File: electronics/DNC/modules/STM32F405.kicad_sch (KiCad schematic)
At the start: 10 parts

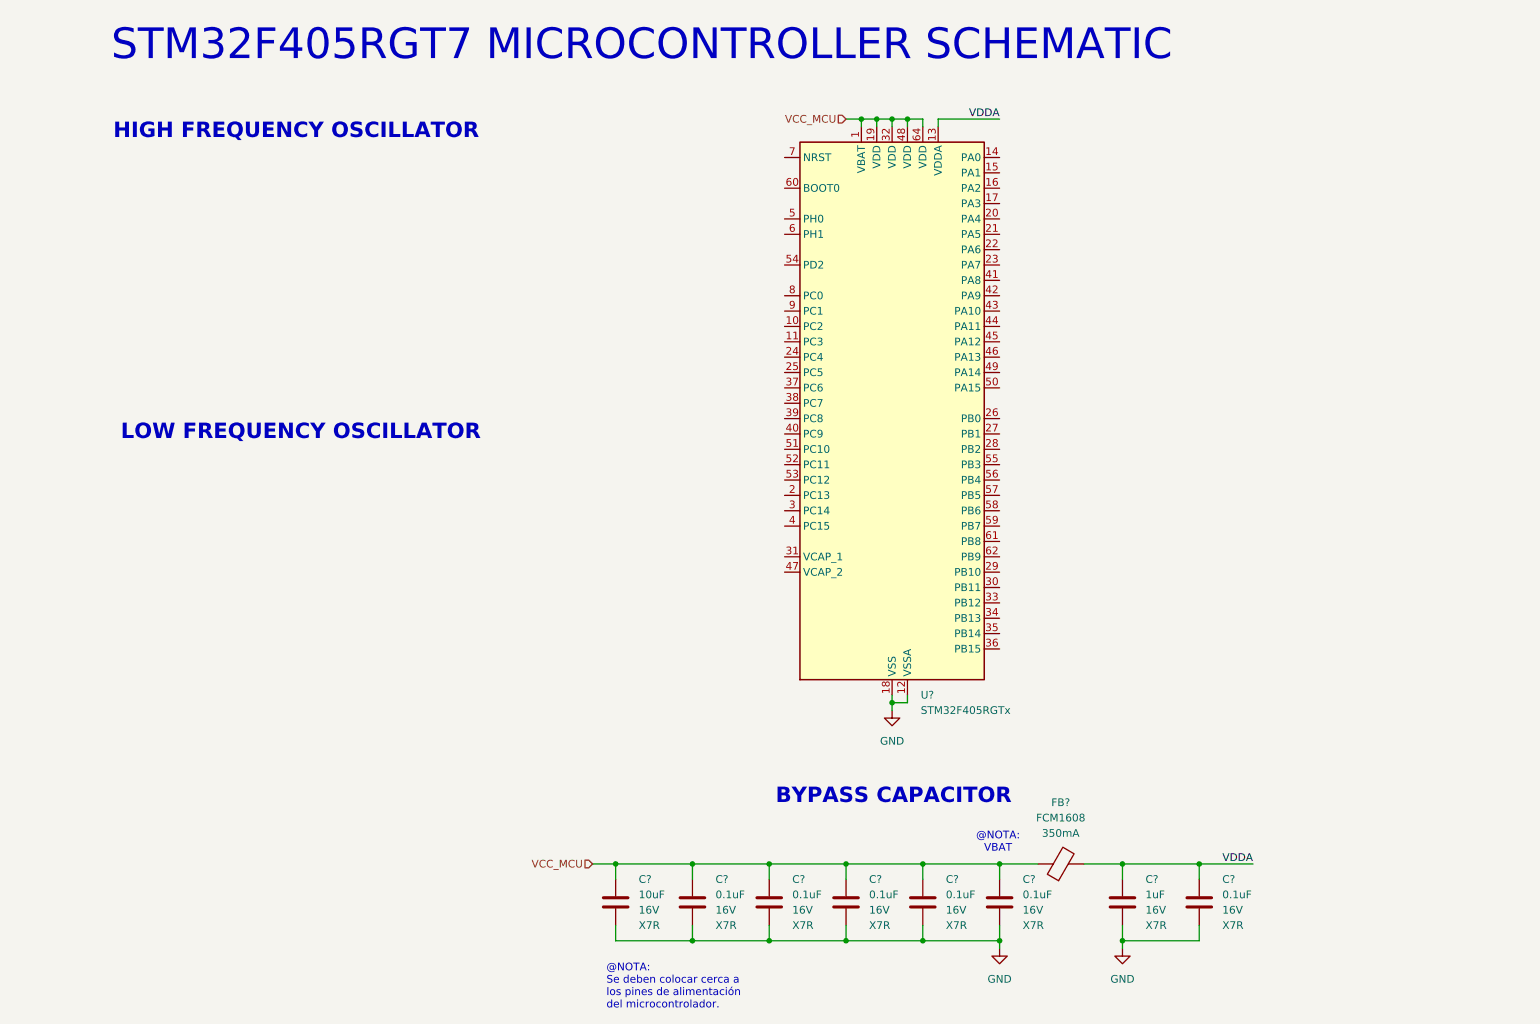
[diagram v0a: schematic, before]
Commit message: Se avanzó con el diseño del DNC y se agregó el modelo 3D del brazo del dron para imprimir
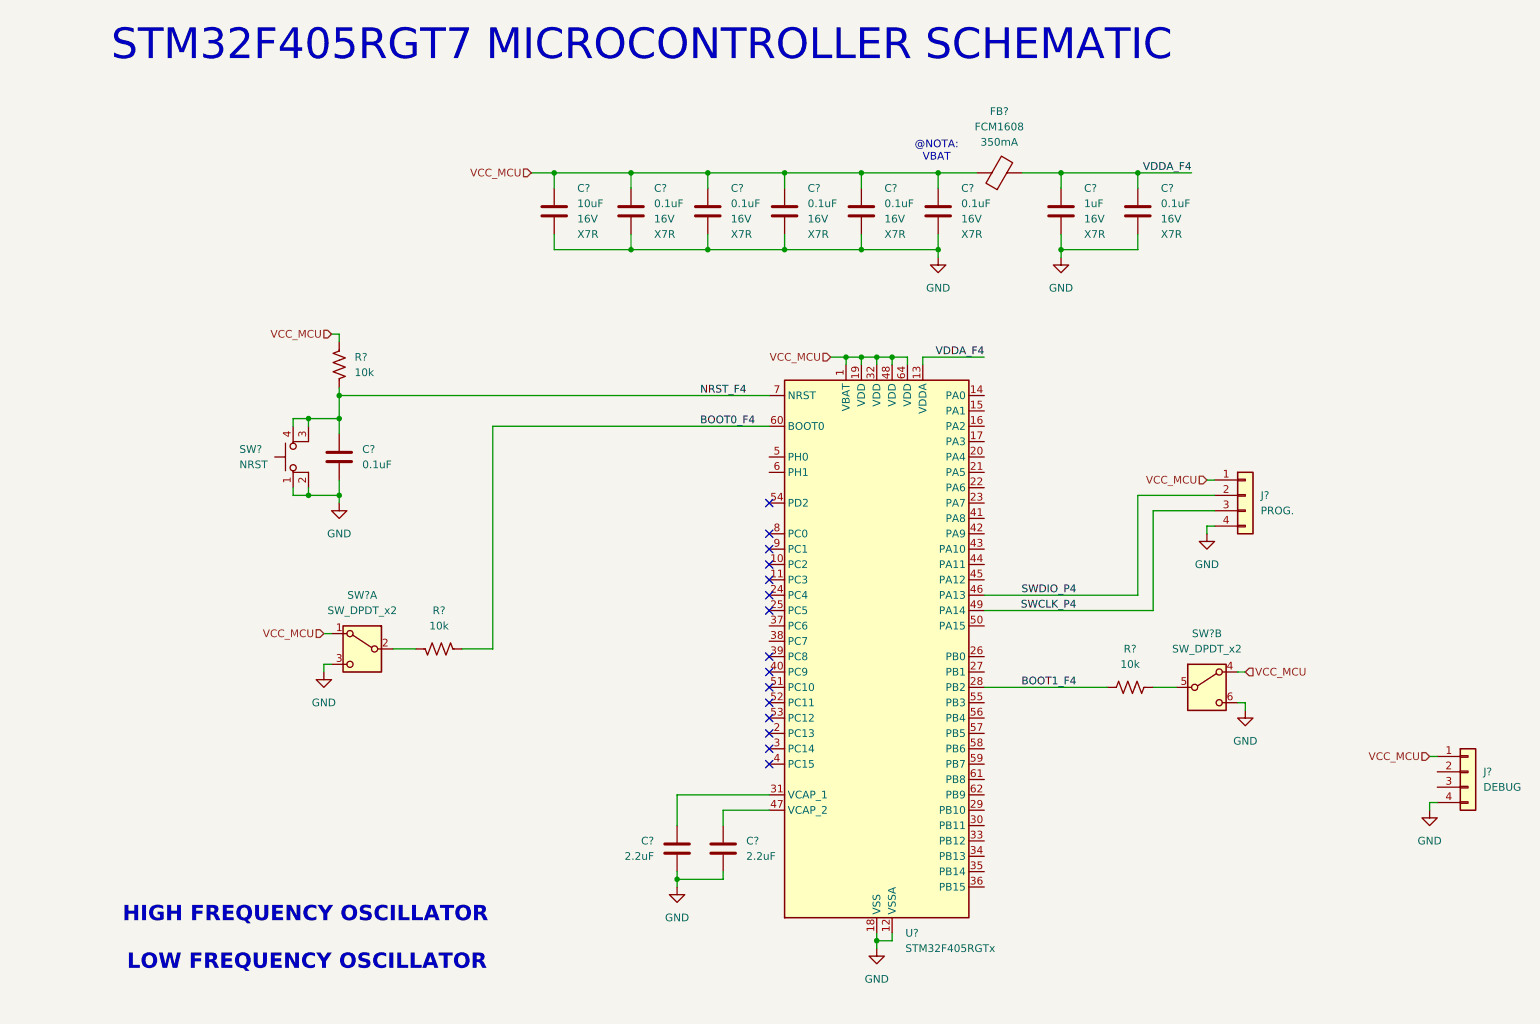
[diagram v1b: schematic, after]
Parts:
- added C? (x2): 2.2uF, symbol Device:C
- added C?: 0.1uF, symbol Device:C
- added J?: PROG., symbol Connector_Generic:Conn_01x04
- added J?: DEBUG, symbol Connector_Generic:Conn_01x04
- added R? (x3): 10k, symbol Device:R_US
- added SW?: NRST, symbol Switch:SW_MEC_5E
- added SW? (x2): SW_DPDT_x2, symbol Switch:SW_DPDT_x2
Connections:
- net GND: now also C?.2, C?.2, C?.2, J?.4 (Pin_4), J?.4 (Pin_4), SW?.1, SW?.2, SW?.3 (C), SW?.6 (C)
- net VCC_MCU: now also J?.1 (Pin_1), J?.1 (Pin_1), R?.1, SW?.1 (A), SW?.4 (A)
- net BOOT1_F4: now reaches U?.28 (PB2)
- net BOOT1_F4: now also R?.1
- net at U?.31 (VCAP_1): now also C?.1
- net SWDIO_P4: now reaches U?.46 (PA13)
- net SWDIO_P4: now also J?.2 (Pin_2)
- net at U?.47 (VCAP_2): now also C?.1
- net SWCLK_P4: now reaches U?.49 (PA14)
- net SWCLK_P4: now also J?.3 (Pin_3)
- net BOOT0_F4: now reaches U?.60 (BOOT0)
- net BOOT0_F4: now also R?.1
- net NRST_F4: now reaches U?.7 (NRST)
- net NRST_F4: now also C?.1, R?.2, SW?.3 (K), SW?.4 (A)
- net VDDA renamed VDDA_F4
- new net: R?.2, SW?.5 (B)
- new net: R?.2, SW?.2 (B)
- no-connect marks 0 -> 15
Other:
- note removed: "@NOTA: Se deben colocar cerca a los pines de alimentación del microcontrolador."
- note removed: "BYPASS CAPACITOR"
- moved on the sheet: C?, FB?, U?
